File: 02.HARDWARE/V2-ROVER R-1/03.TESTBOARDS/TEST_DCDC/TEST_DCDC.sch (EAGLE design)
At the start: 56 parts, among them J1 FEMALE 2x3, J2 OSTVN03A150, J3 OSTVN03A150, J4 OSTVN03A150, J5 ACJS-MHDR, Q1 PJA3416AE_R1_00001, Q2 PJA3416AE_R1_00001, Q3 PJA3416AE_R1_00001, Q4 310mA/60V/1.6Ω, U1 MCP4725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

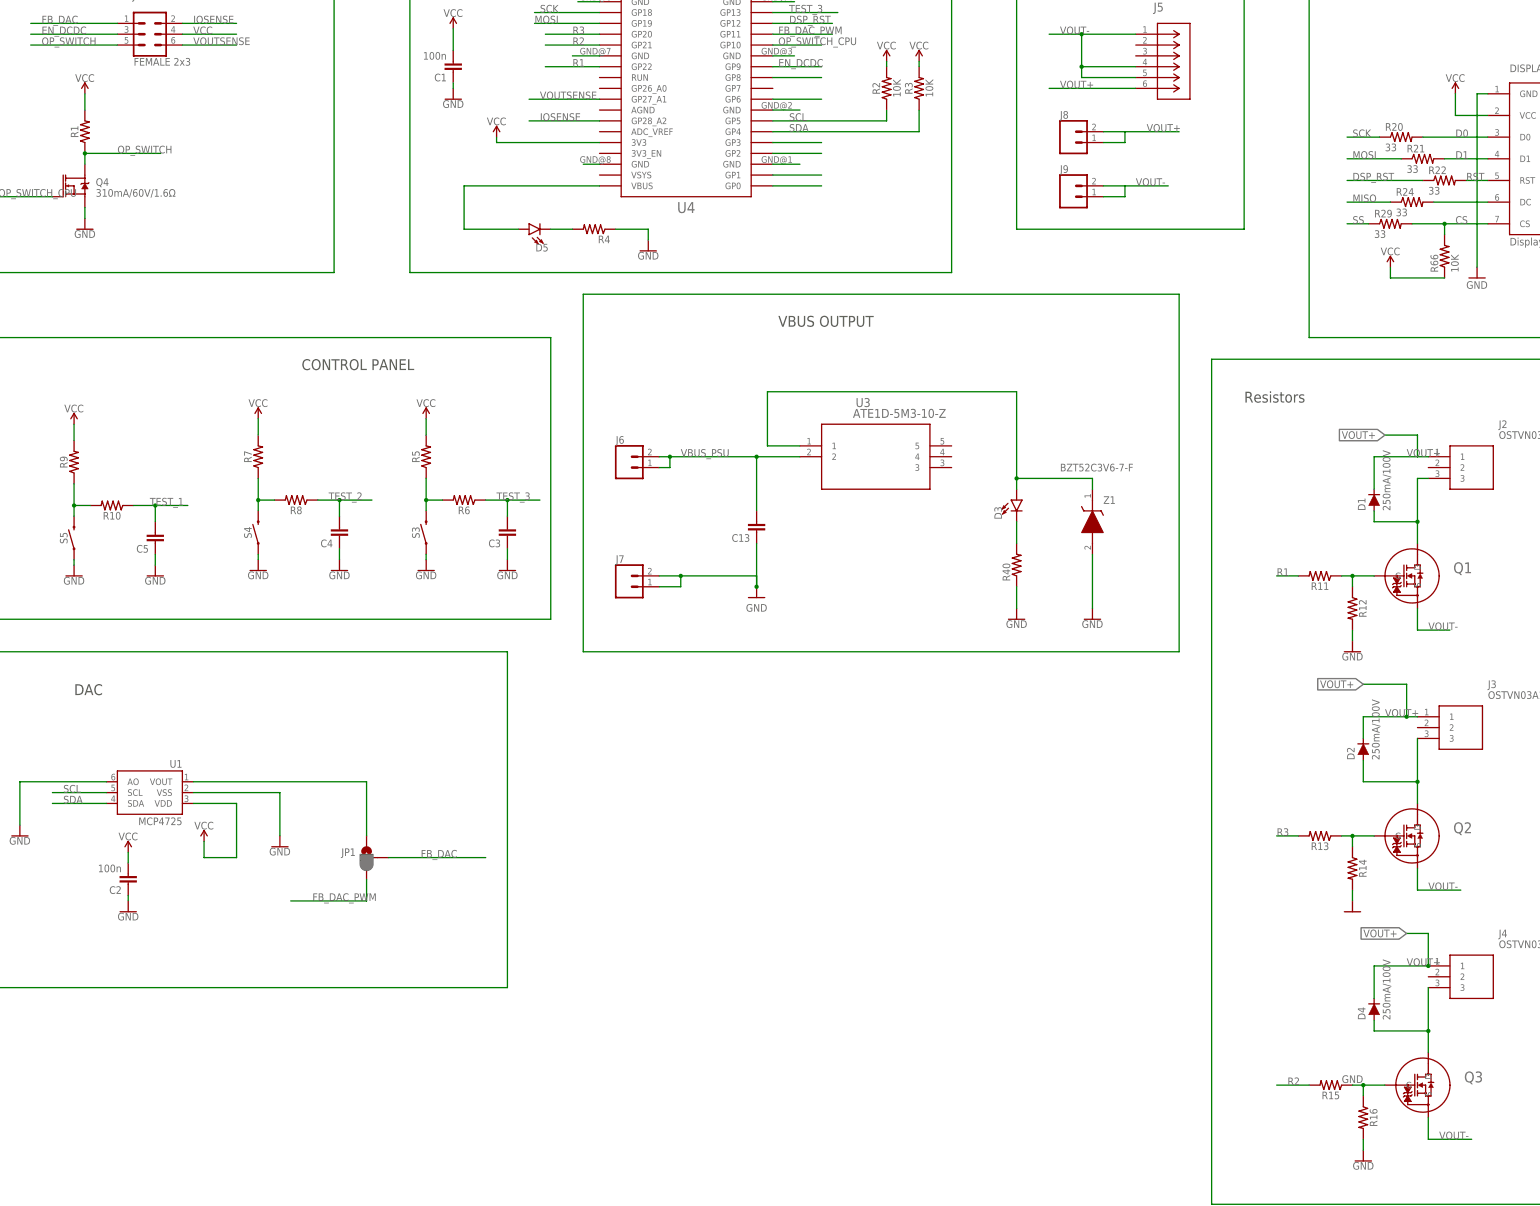
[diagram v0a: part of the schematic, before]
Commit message: Asignacion de Valores a los componentes pasivos de las tarjetas de Testeo. Actualziacion de las BOMs.
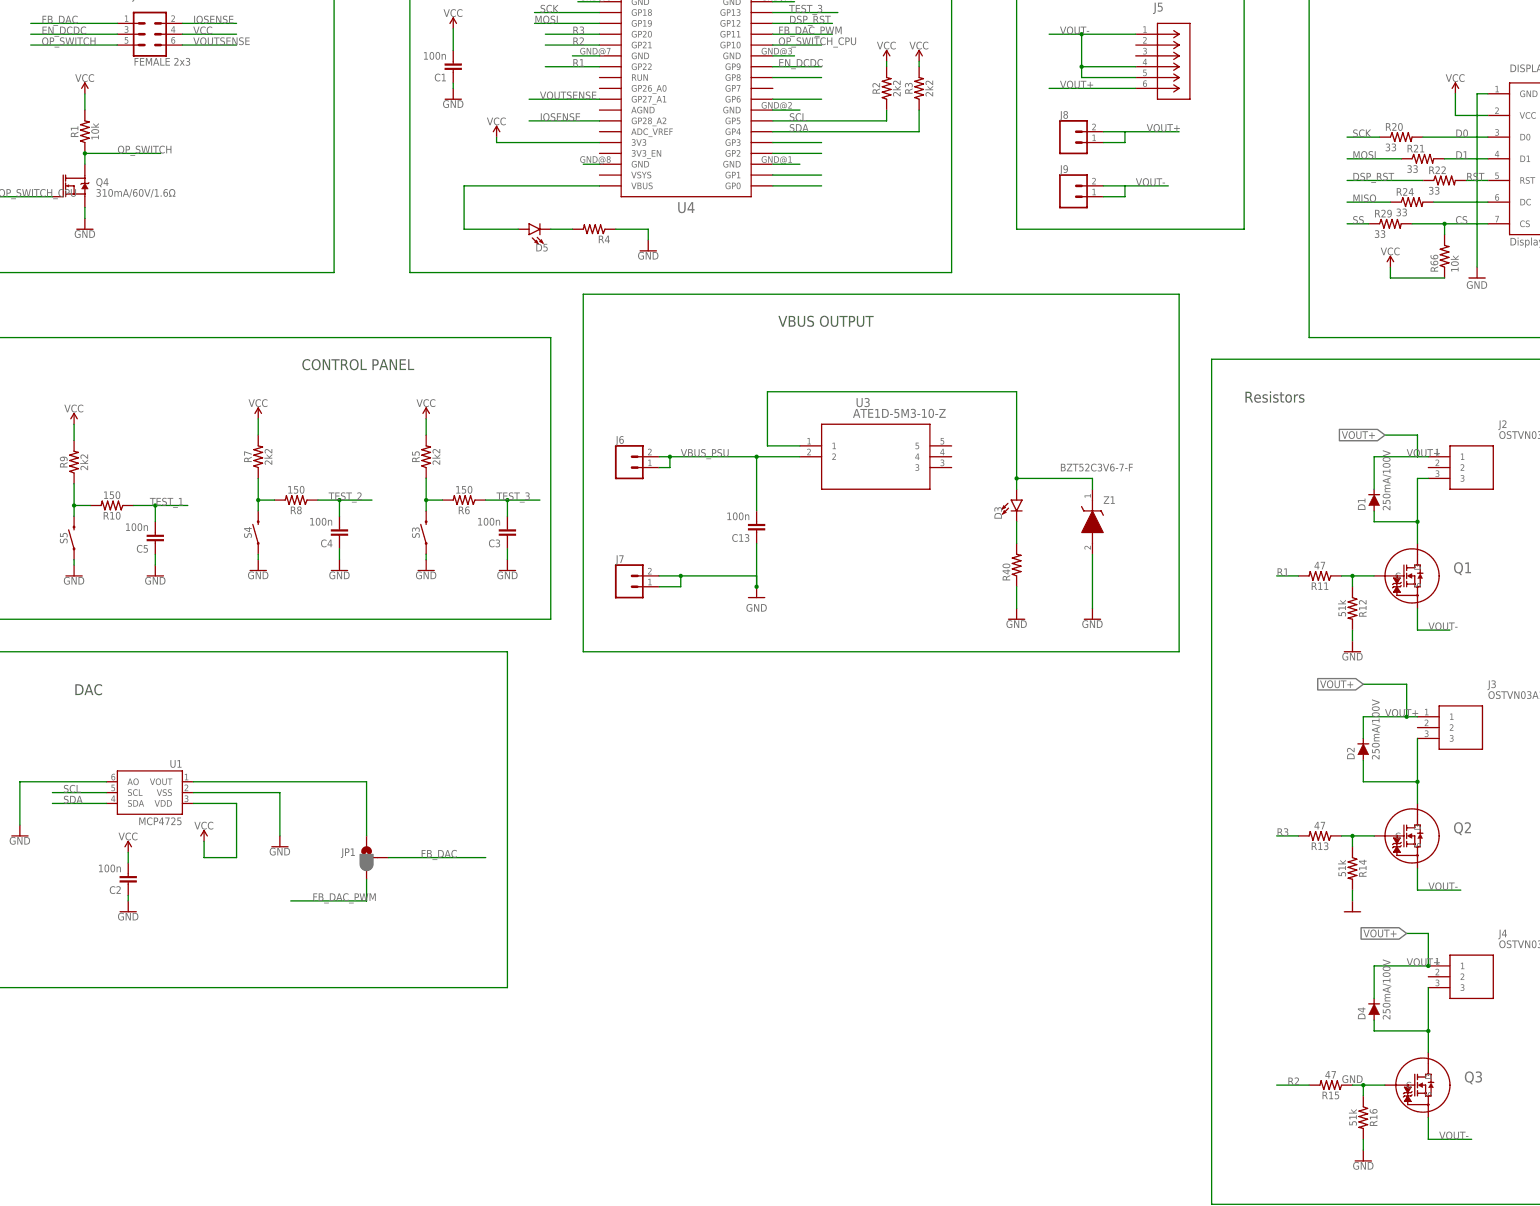
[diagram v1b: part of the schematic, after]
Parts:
- C13, C3, C4, C5: value (none) -> 100n
- R1: value (none) -> 10k
- R10, R6, R8: value (none) -> 150
- R11, R13, R15: value (none) -> 47
- R12, R14, R16: value (none) -> 51k
- R2, R3: value 10K -> 2k2
- R20, R21, R22, R24, R29: device SparkFun:RESISTOR0805-RES -> SparkFun-Resistors:RESISTOR0805
- R4, R40: value 10K -> 360; device SparkFun:RESISTOR0805-RES -> SparkFun-Resistors:RESISTOR0805
- R5, R7, R9: value (none) -> 2k2
- R66: value 10K -> 10k; device SparkFun:RESISTOR0805-RES -> SparkFun-Resistors:RESISTOR0805
